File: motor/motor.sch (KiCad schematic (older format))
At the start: 13 parts, among them J1 power, J2 from switches, J3 motor, J4 towards uC, U1 L293D

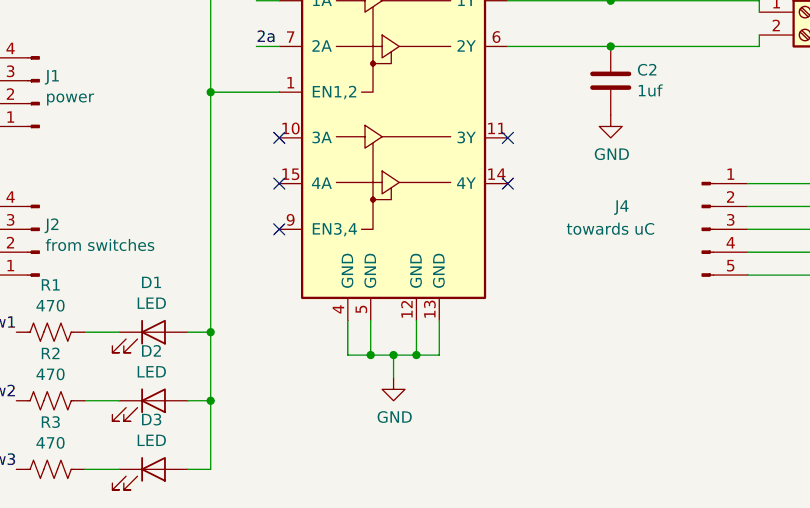
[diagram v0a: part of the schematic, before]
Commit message: changed LEds from 3mm to 5mm;added Status LED to motor-module
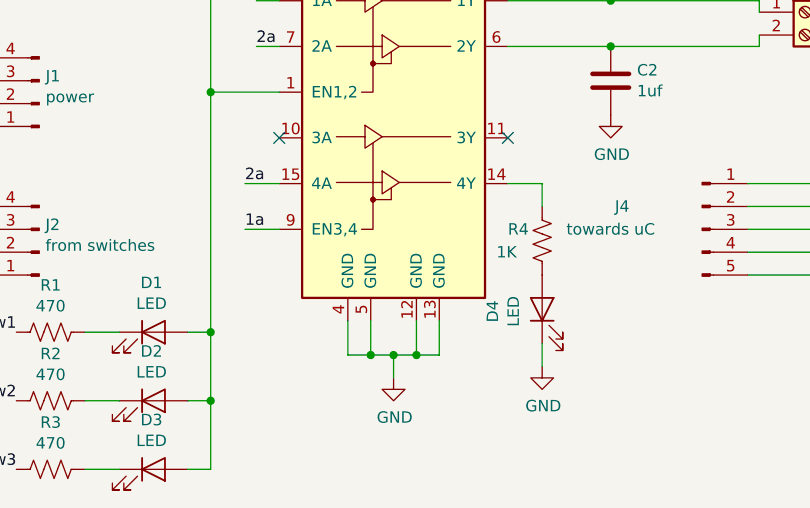
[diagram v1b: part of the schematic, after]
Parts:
- added D4: LED, LEDs:LED_D5.0mm, symbol Device:LED
- added R4: 1K, Resistors_THT:R_Axial_DIN0207_L6.3mm_D2.5mm_P5.08mm_Vertical, symbol Device:R_US
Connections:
- net 1a: now also U1.9 (EN3,4)
- net 2a: now also U1.15 (4A)
- net GND: now also D4.1 (K)
- net at U1.14 (4Y): now also R4.1
- new net: D4.2 (A), R4.2
- no-connect marks 6 -> 3
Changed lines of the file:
@@
 EESchema Schematic File Version 4
+LIBS:motor-cache
 EELAYER 26 0
 EELAYER END
@@
 $EndComp
 NoConn ~ 6050 3800
-NoConn ~ 6050 4000
-NoConn ~ 5050 4000
 NoConn ~ 5050 3800
-NoConn ~ 5050 4200
 $Comp
 L power:+5V #PWR0102
@@
 Text Label 3900 5250 2    50   ~ 0
 sw3
+Wire Wire Line
+	4900 4000 5050 4000
+Wire Wire Line
+	5050 4200 4900 4200
+Text Label 4900 4000 0    50   ~ 0
+2a
+Text Label 4900 4200 0    50   ~ 0
+1a
+$Comp
+L Device:R_US R4
+U 1 1 5C332B9A
+P 6200 4250
+F 0 "R4" H 6050 4300 50  0000 L CNN
+F 1 "1K" H 6000 4200 50  0000 L CNN
+F 2 "Resistors_THT:R_Axial_DIN0207_L6.3mm_D2.5mm_P5.08mm_Vertical" V 6240 4240 50  0001 C CNN
+F 3 "~" H 6200 4250 50  0001 C CNN
+	1    6200 4250
+	1    0    0    -1
+$EndComp
+Wire Wire Line
+	6050 4000 6200 4000
+Wire Wire Line
+	6200 4000 6200 4100
+$Comp
+L Device:LED D4
+U 1 1 5C333823
+P 6200 4550
+F 0 "D4" H 6191 4766 50  0000 C CNN
+F 1 "LED" H 6191 4675 50  0000 C CNN
+F 2 "LEDs:LED_D5.0mm" H 6200 4550 50  0001 C CNN
+F 3 "~" H 6200 4550 50  0001 C CNN
+	1    6200 4550
+	0    -1   -1   0
+$EndComp
+$Comp
+L power:GND #PWR0106
+U 1 1 5C3338C6
+P 6200 4800
+F 0 "#PWR0106" H 6200 4550 50  0001 C CNN
+F 1 "GND" H 6205 4627 50  0000 C CNN
+F 2 "" H 6200 4800 50  0001 C CNN
+F 3 "" H 6200 4800 50  0001 C CNN
+	1    6200 4800
+	1    0    0    -1
+$EndComp
+Wire Wire Line
+	6200 4700 6200 4800
 $EndSCHEMATC

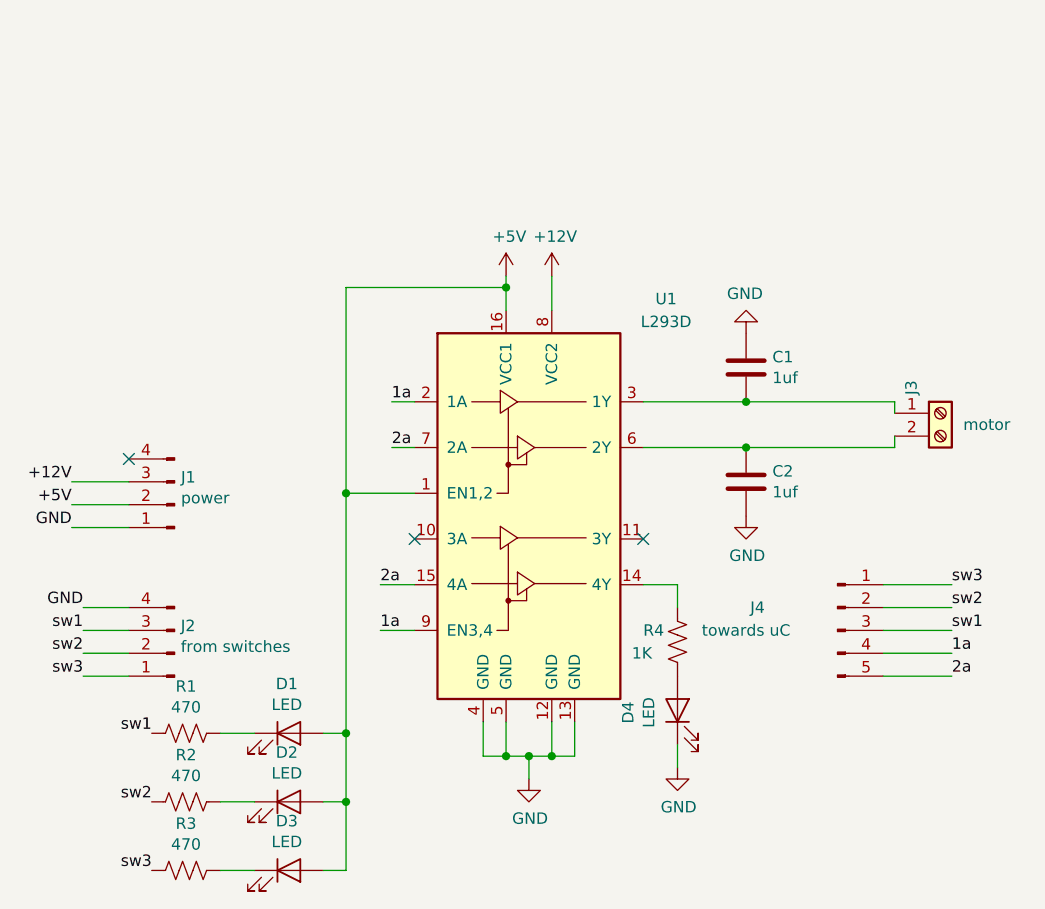
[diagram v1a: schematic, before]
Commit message: added indicator LED's in heater module; added proper markings in motor module.
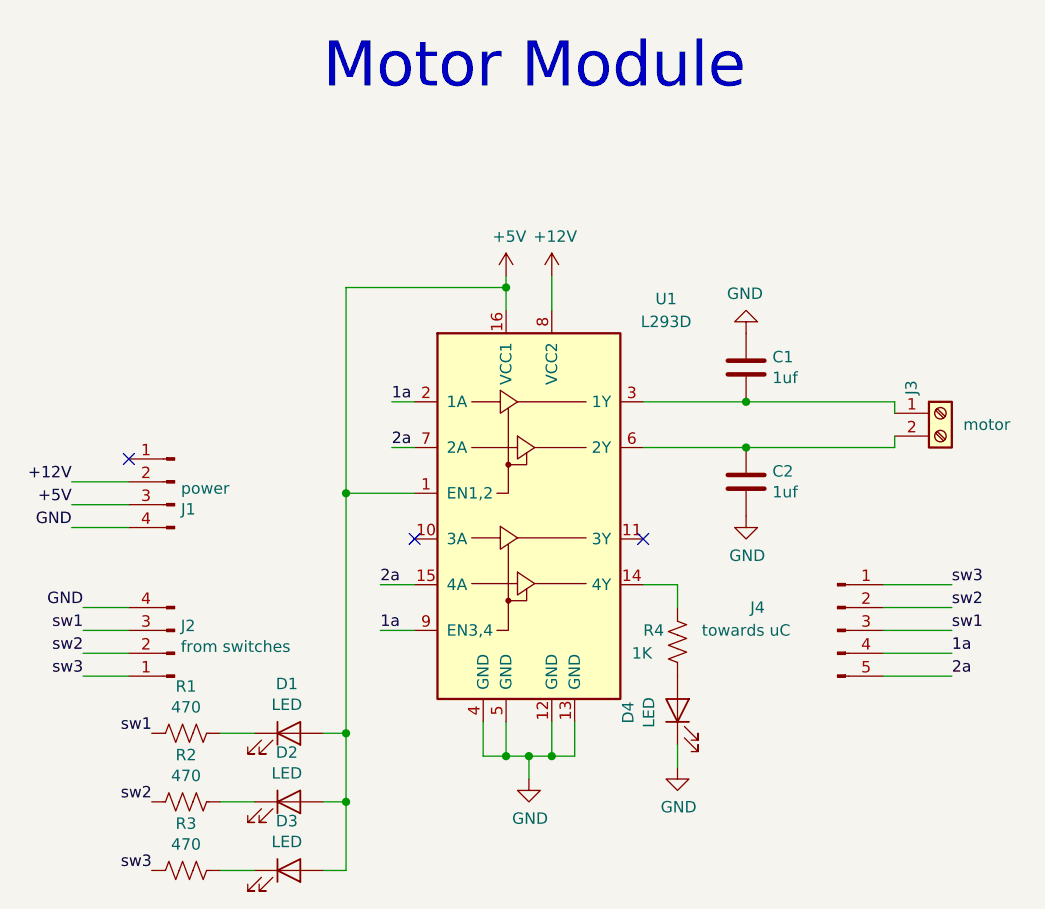
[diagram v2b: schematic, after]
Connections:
- net +12V: now also J1.2 (Pin_2); no longer J1.3 (Pin_3)
- net +5V: now also J1.3 (Pin_3); no longer J1.2 (Pin_2)
- net GND: now also J1.4 (Pin_4); no longer J1.1 (Pin_1)
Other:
- note added: "Motor Module"
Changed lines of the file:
@@
 L Connector:Conn_01x04_Male J1
 U 1 1 5C2E1CA4
-P 4000 3650
-F 0 "J1" H 3972 3530 50  0000 R CNN
-F 1 "power" H 3972 3621 50  0000 R CNN
-F 2 "Connectors_JST:JST_EH_B04B-EH-A_04x2.50mm_Straight" H 4000 3650 50  0001 C CNN
-F 3 "~" H 4000 3650 50  0001 C CNN
-	1    4000 3650
-	-1   0    0    1
-$EndComp
-Wire Wire Line
-	3800 3750 3550 3750
+P 4000 3550
+F 0 "J1" H 3972 3430 50  0000 R CNN
+F 1 "power" H 3972 3521 50  0000 R CNN
+F 2 "Connectors_JST:JST_EH_B04B-EH-A_04x2.50mm_Straight" H 4000 3550 50  0001 C CNN
+F 3 "~" H 4000 3550 50  0001 C CNN
+	1    4000 3550
+	-1   0    0    -1
+$EndComp
 Wire Wire Line
 	3800 3650 3550 3650
@@
 Text Label 3550 3750 2    50   ~ 0
 GND
-NoConn ~ 3800 3450
 Wire Wire Line
 	7100 4000 7400 4000
@@
 Wire Wire Line
 	6200 4700 6200 4800
+Text Notes 4650 1850 0    197  ~ 0
+Motor Module
+Wire Wire Line
+	3800 3750 3550 3750
+NoConn ~ 3800 3450
 $EndSCHEMATC

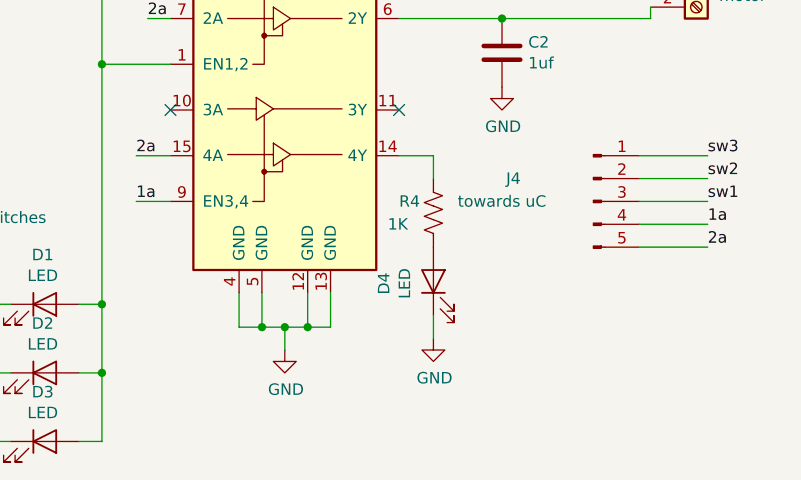
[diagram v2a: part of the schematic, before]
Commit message: mounting holes in motor, extra pins in traffic, corrections in labels
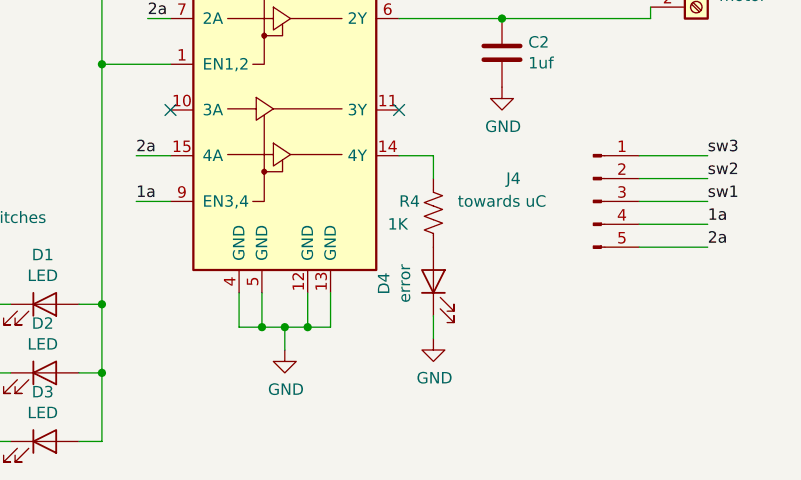
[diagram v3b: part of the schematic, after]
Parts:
- D4: value LED -> error
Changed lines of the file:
@@
 P 6200 4550
 F 0 "D4" H 6191 4766 50  0000 C CNN
-F 1 "LED" H 6191 4675 50  0000 C CNN
+F 1 "error" H 6191 4675 50  0000 C CNN
 F 2 "LEDs:LED_D5.0mm" H 6200 4550 50  0001 C CNN
 F 3 "~" H 6200 4550 50  0001 C CNN
